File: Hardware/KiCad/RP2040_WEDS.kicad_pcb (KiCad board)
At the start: 2 copper layers, 55 x 66 mm, 75 parts, among them J1 Barrel_Jack_Switch_Pin3Ring, J2 Conn_01x02_Male, J3 I2C Soil Header, J4 LiPo Batt, J5 Analog Soil Header, J6 USB Header, J7 Conn_02x05_Odd_Even, J8 SMA-J-P-H-RA-TH1, Q1 Q_PMOS_DGS, Q2 Q_PMOS_DGS, SW1 SW_Push, SW2 SW_Push, SW3 SW_Push, U1 RP2040, U2 MCP73831-2-OT, U3 W25Q128JVS, U4 BME280, U5 AP2112K-3.3, U6 LoRa-E5, U7 TPL5110, Y1 Crystal_GND24

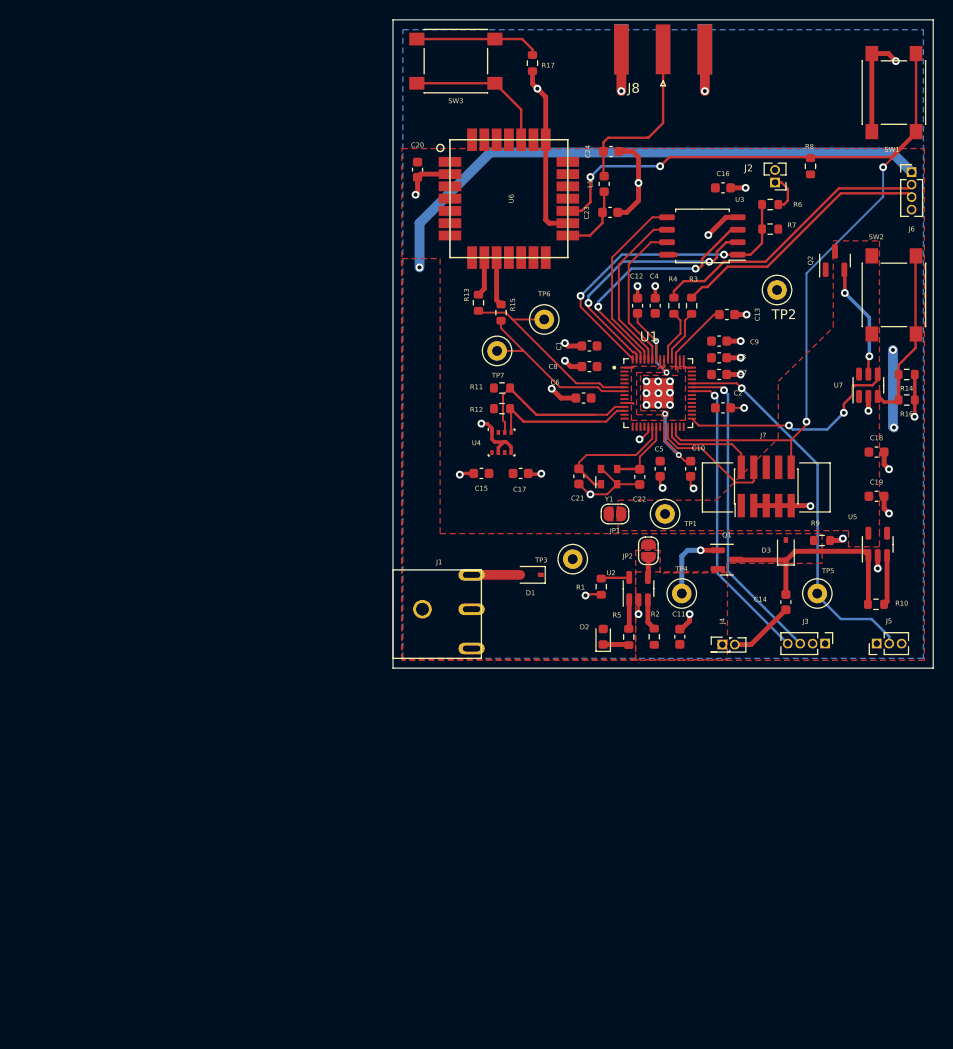
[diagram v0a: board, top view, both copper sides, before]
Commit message: added thermal relief to fill zones
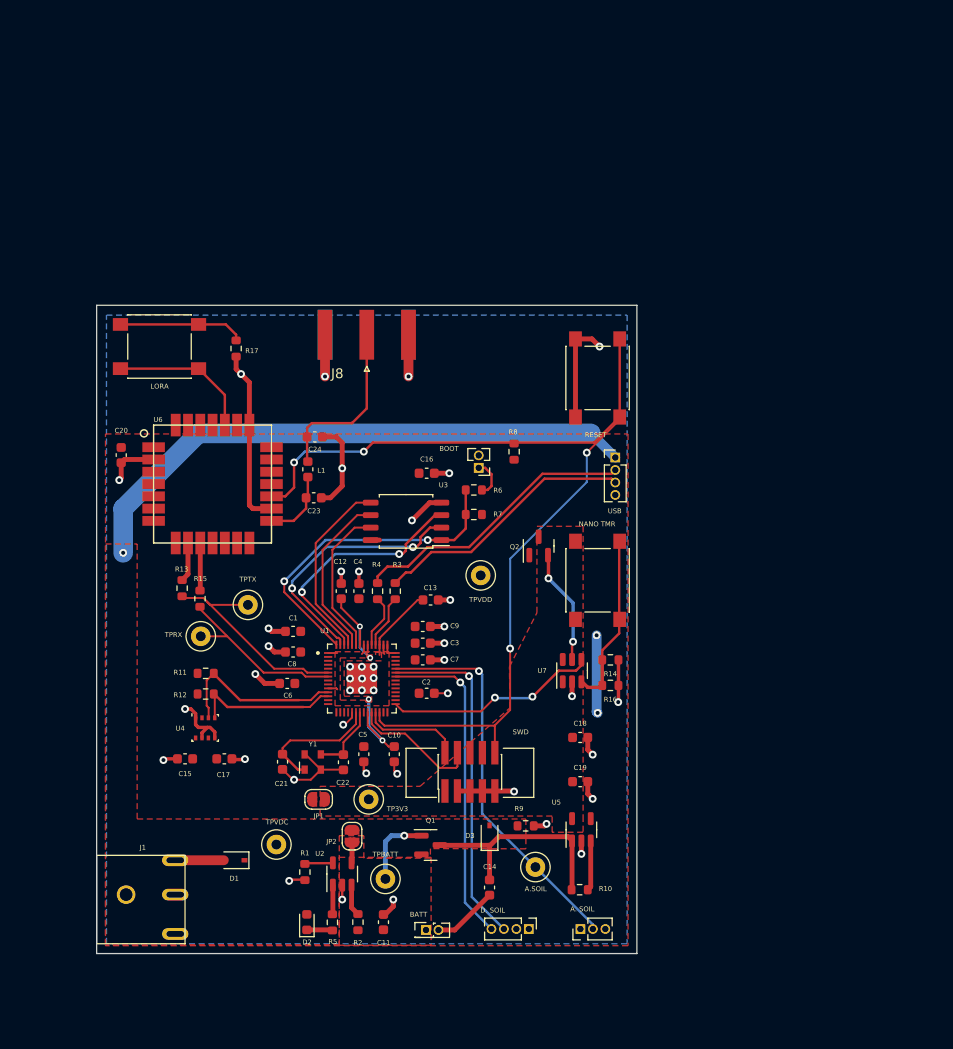
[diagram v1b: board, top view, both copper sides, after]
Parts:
- A. SOIL: renamed from J5
- D. SOIL: renamed from J3
- NANO TMR: renamed from SW2
- moved R15 42.3 mm to (130.3, 97.9)
- moved BOOT 41.9 mm to (158.7, 84.6)
- moved C12 41.9 mm to (144.7, 97.2)
- moved C21 41.9 mm to (138.8, 114.5)
- moved C6 41.9 mm to (139.2, 106.6)
- moved R10 41.9 mm to (169.0, 127.6)
- moved R14 41.9 mm to (172.1, 104.2)
- moved R3 41.9 mm to (150.2, 97.2)
- moved R6 41.9 mm to (158.2, 86.9)
- moved R7 41.9 mm to (158.2, 89.4)
- moved R9 41.9 mm to (163.5, 121.1)
- moved TPTX 41.9 mm to (135.2, 98.6)
- moved USB 41.9 mm to (172.6, 83.6)
- moved C10 41.9 mm to (150.1, 113.8)
- moved C20 41.9 mm to (122.3, 83.3)
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- renumbered TP5 to A.SOIL, J4 to BATT, J2 to BOOT, SW3 to LORA, SW1 to RESET, J7 to SWD, TP1 to TP3V3, TP4 to TPBATT, TP7 to TPRX, TP6 to TPTX, TP3 to TPVDC, TP2 to TPVDD, J6 to USB
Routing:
- net SCL_SOIL: track 32.4 -> 34.8 mm
- net SDA_SOIL: track 30.8 -> 33.2 mm
- net DONE: track 23.0 -> 21.8 mm
- net LORA_TX: track 21.3 -> 22.4 mm

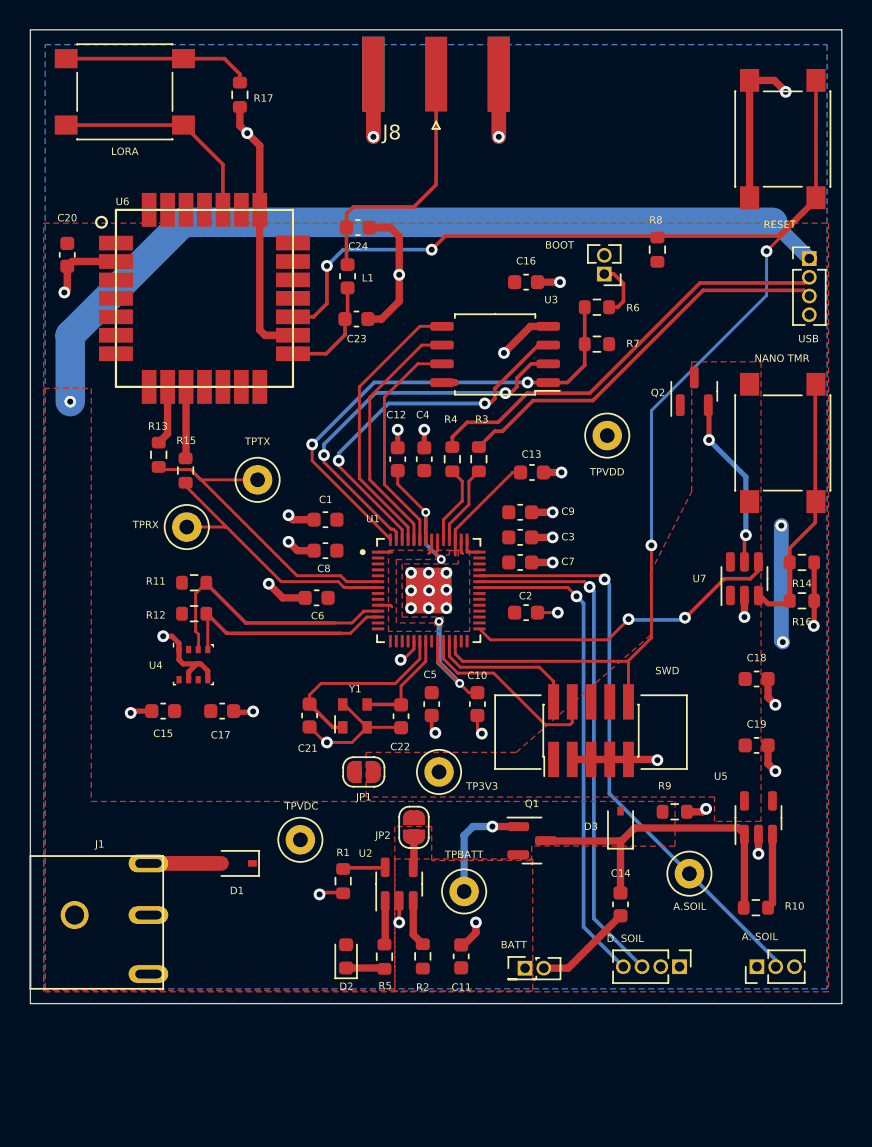
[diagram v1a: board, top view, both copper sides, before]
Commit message: changed the size of headers form 1.27 to 2.54mm
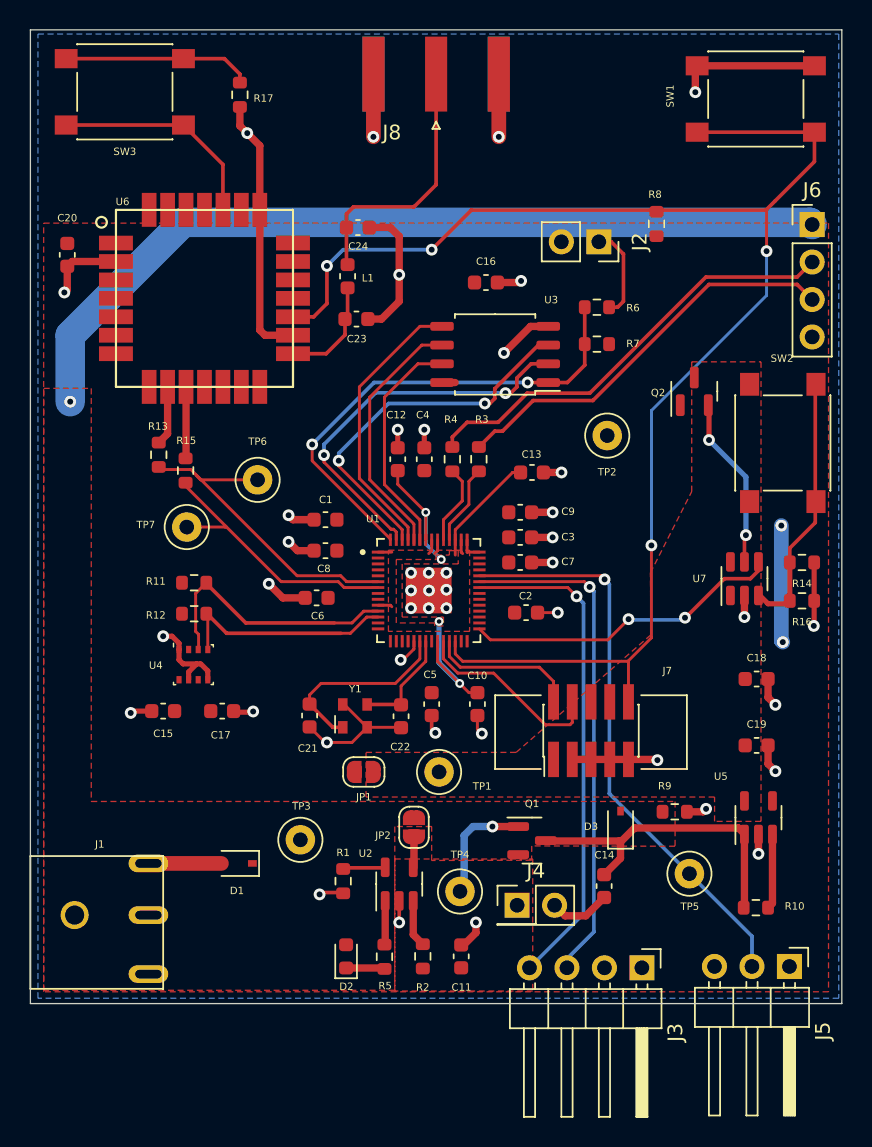
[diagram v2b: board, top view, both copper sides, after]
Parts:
- J2: renamed from BOOT; footprint Connector_PinHeader_1.27mm:PinHeader_1x02_P1.27mm_Vertical -> Connector_PinSocket_2.54mm:PinSocket_1x02_P2.54mm_Vertical
- J3: renamed from D. SOIL; footprint Connector_PinHeader_1.27mm:PinHeader_1x04_P1.27mm_Vertical -> Connector_PinHeader_2.54mm:PinHeader_1x04_P2.54mm_Horizontal
- J4: renamed from BATT; footprint Connector_PinHeader_1.27mm:PinHeader_2x01_P1.27mm_Vertical -> Connector_PinHeader_2.54mm:PinHeader_2x01_P2.54mm_Vertical
- J5: renamed from A. SOIL; footprint Connector_PinHeader_1.27mm:PinHeader_1x03_P1.27mm_Vertical -> Connector_PinHeader_2.54mm:PinHeader_1x03_P2.54mm_Horizontal
- J6: renamed from USB; footprint Connector_PinHeader_1.27mm:PinHeader_1x04_P1.27mm_Vertical -> Connector_PinHeader_2.54mm:PinHeader_1x04_P2.54mm_Vertical
- SW2: renamed from NANO TMR
- moved J4 4.30 mm to (152.8, 127.4)
- moved SW1 3.27 mm to (169.0, 72.7), turned to 180 degrees
- moved C16 2.72 mm to (150.7, 85.2)
- moved J3 2.55 mm to (161.3, 131.6)
- moved J6 2.31 mm to (172.8, 81.2)
- moved J2 2.22 mm to (158.4, 82.4), turned to -90 degrees
- moved J5 2.20 mm to (171.3, 131.5), turned to -90 degrees
- moved R8 1.75 mm to (162.3, 81.2)
- moved C14 1.66 mm to (158.7, 126.1)
- moved TP4 0.28 mm to (148.9, 126.5)
- renumbered SWD to J7, RESET to SW1, LORA to SW3, TP3V3 to TP1, TPVDD to TP2, TPVDC to TP3, TPBATT to TP4, A.SOIL to TP5, TPTX to TP6, TPRX to TP7
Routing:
- net GND: track 127.4 -> 124.1 mm
- net /~{USB_BOOT}: track 3.91 -> 6.36 mm
- net RESET: track 100.5 -> 102.0 mm
- net Net-(C14-Pad1): track 22.5 -> 21.7 mm
- net VDC: track 58.8 -> 58.0 mm
- net SOIL_SIG: track 39.6 -> 39.0 mm
- net USB_DP: track 29.4 -> 30.0 mm
- net USB_DN: track 27.0 -> 27.6 mm
- net SCL_SOIL: track 34.8 -> 34.3 mm

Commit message: fixed component values
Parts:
- removed JP2: SolderJumper_2_Open, Jumper:SolderJumper-2_P1.3mm_Open_RoundedPad1.0x1.5mm
- removed R10: 10k, Resistor_SMD:R_0603_1608Metric
- removed R2: 0, Resistor_SMD:R_0603_1608Metric
- removed TP4, TP5: TestPoint, TestPoint:TestPoint_Loop_D1.80mm_Drill1.0mm_Beaded
- added J9: Solar, Connector_PinHeader_2.54mm:PinHeader_1x02_P2.54mm_Horizontal, F.Cu at (122.2, 119.9)
- C11, C19: value 10uF -> 4.7uF
- C18: value 10uF -> 1uF
- J4: moved to B.Cu
- R5: value 10k -> 470
- U5: value AP2112K-3.3 -> XC6210B332MR
- moved C19 24.8 mm to (144.9, 122.0), turned to 180 degrees
- moved TP3 7.94 mm to (134.1, 129.8)
- moved D2 7.48 mm to (139.4, 123.6)
- moved J4 7.32 mm to (146.7, 131.4), turned to 180 degrees
- moved C14 7.01 mm to (165.4, 124.0), turned to 90 degrees
- moved R5 5.66 mm to (140.5, 126.3), turned to 0 degrees
- moved C18 5.09 mm to (170.3, 117.0)
- moved C11 4.84 mm to (144.7, 128.7), turned to 180 degrees
- moved Q1 2.96 mm to (151.7, 125.0), turned to 180 degrees
- moved J7 2.95 mm to (160.8, 115.5)
- moved R1 2.19 mm to (141.4, 123.6), turned to -90 degrees
- moved D3 2.01 mm to (159.2, 124.0)
- moved R9 1.60 mm to (162.0, 121.7)
- moved J2 1.38 mm to (158.3, 83.8)
- moved U5 1.22 mm to (170.3, 121.0)
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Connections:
- C19 pad 1: +3V3 -> VDC
- U2 pad 3: Net-(R2-Pad2) -> +BATT
- U2 pad 4: Net-(JP2-Pad1) -> VDC
- U5 pad 3: Net-(R10-Pad1) -> Net-(C14-Pad1)
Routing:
- net +BATT: track 7.76 -> 0.00 mm, vias 1 -> 0
- net Net-(R10-Pad1): track 5.12 -> 0.00 mm
- net Net-(R2-Pad2): track 3.24 -> 0.00 mm
- net +3V3: track 0.14 -> 3.14 mm
- net SWD_CLK: track 13.2 -> 15.9 mm
- net Net-(C14-Pad1): track 21.7 -> 23.9 mm
- net RESET: track 102.0 -> 104.1 mm
- net SWD_DIO: track 10.2 -> 12.3 mm
- net Net-(JP2-Pad1): track 2.05 -> 0.00 mm
- net VDC: track 58.0 -> 60.0 mm
- net /~{USB_BOOT}: track 6.36 -> 4.51 mm
- net GND: track 124.1 -> 122.8 mm, vias 44 -> 42
- net Net-(D2-Pad1): track 2.73 -> 2.03 mm
- net Net-(R5-Pad2): track 3.02 -> 2.45 mm

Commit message: Version 1.2 board
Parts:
- removed J1: Barrel_Jack_Switch_Pin3Ring, 54-00125:54-00125
- added D4: LED, LED_SMD:LED_0603_1608Metric, F.Cu at (125.5, 131.3)
- added R10: 0, Resistor_SMD:R_0603_1608Metric, F.Cu at (148.0, 123.4)
- added R18: 0, Resistor_SMD:R_0603_1608Metric, F.Cu at (160.7, 128.6)
- added R19: 0, Resistor_SMD:R_0603_1608Metric, F.Cu at (170.5, 128.6)
- added R2: 0, Resistor_SMD:R_0603_1608Metric, F.Cu at (148.1, 127.8)
- added R20: 0, Resistor_SMD:R_0603_1608Metric, F.Cu at (122.2, 94.4)
- added R21: 0, Resistor_SMD:R_0603_1608Metric, F.Cu at (169.1, 117.1)
- added R22: 470, Resistor_SMD:R_0603_1608Metric, F.Cu at (122.3, 131.3)
- added TP4: GND, TestPoint:TestPoint_Loop_D1.80mm_Drill1.0mm_Beaded, F.Cu at (130.5, 131.5)
- added TP5: 1V1, TestPoint:TestPoint_Loop_D1.80mm_Drill1.0mm_Beaded, F.Cu at (158.9, 95.4)
- added TP8: Q1, TestPoint:TestPoint_Loop_D1.80mm_Drill1.0mm_Beaded, F.Cu at (160.8, 125.0)
- J2: value Conn_01x02_Male -> USB BOOT
- J7: value Conn_02x05_Odd_Even -> SWD Header; footprint Connector_PinHeader_1.27mm:PinHeader_2x05_P1.27mm_Vertical_SMD -> Connector_PinHeader_1.27mm:PinHeader_2x05_P1.27mm_Vertical
- J8: value SMA-J-P-H-RA-TH1 -> SMA-Conn
- J9: value Solar -> Solar Panel Input; moved to B.Cu
- JP1: value SolderJumper_2_Open -> Power Isolation
- R11, R12: value 10k -> 4.7k
- TP1: value TestPoint -> 3V3
- TP2: value TestPoint -> VDD
- TP3: value TestPoint -> VDC
- TP6: value TestPoint -> LoRa_TX
- TP7: value TestPoint -> LoRa_RX
- moved R9 9.99 mm to (152.0, 121.3), turned to 180 degrees
- moved C17 9.06 mm to (126.3, 107.9), turned to 90 degrees
- moved D2 7.85 mm to (140.9, 131.3)
- moved TP2 5.75 mm to (158.9, 101.3)
- moved R5 5.30 mm to (138.7, 131.3), turned to 90 degrees
- moved R12 5.16 mm to (134.1, 111.7)
- moved J9 4.68 mm to (122.2, 124.6)
- moved R11 4.14 mm to (134.1, 108.2)
- moved TP7 3.79 mm to (133.7, 103.6)
- moved C15 3.48 mm to (126.3, 111.8), turned to -90 degrees
- moved J7 3.21 mm to (163.5, 117.2), turned to 180 degrees
- moved C18 3.03 mm to (169.1, 114.2)
- moved D3 3.01 mm to (156.1, 123.9)
- moved TP3 2.00 mm to (135.1, 131.5)
- moved U4 1.73 mm to (129.6, 109.9), turned to -90 degrees
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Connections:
- C9 pad 1: VDD -> GND
- C9 pad 2: GND -> VDD
- D1 pad 2: Net-(D1-Pad2) -> Net-(J9-Pad1)
- D2 pad 2: VDC -> Net-(U2-Pad1)
- J3 pad 1: VDD -> Net-(J3-Pad1)
- J5 pad 1: VDD -> Net-(J5-Pad1)
- J6 pad 1: VDC -> Net-(J6-Pad1)
- J9 pad 1: VDC -> Net-(J9-Pad1)
- R5 pad 2: Net-(R5-Pad2) -> GND
- U1 pad 4: unconnected-(U1-Pad4) -> NRST
- U2 pad 1: Net-(R5-Pad2) -> Net-(U2-Pad1)
- U2 pad 3: +BATT -> Net-(U2-Pad3)
- U2 pad 4: VDC -> Net-(U2-Pad4)
- U5 pad 5: +3V3 -> Net-(U5-Pad5)
- U6 pad 17: RESET -> NRST
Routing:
- net VDC: track 60.0 -> 0.00 mm, vias 1 -> 0
- net Net-(J6-Pad1): track 0.00 -> 57.1 mm, vias 0 -> 1
- net RESET: track 104.1 -> 71.4 mm, vias 4 -> 2
- net NRST: track 0.00 -> 23.1 mm, vias 0 -> 2
- net Net-(J9-Pad1): track 0.00 -> 10.6 mm
- net +1V1: track 26.6 -> 33.6 mm
- net Net-(U2-Pad1): track 0.00 -> 6.22 mm
- net SWD_DIO: track 12.3 -> 17.8 mm, vias 0 -> 1
- net Net-(D1-Pad2): track 4.95 -> 0.00 mm
- net SDA: track 18.0 -> 13.9 mm
- net GND: track 122.8 -> 118.8 mm, vias 42 -> 44
- net Net-(D4-Pad1): track 0.00 -> 3.22 mm
- net Net-(U5-Pad5): track 0.00 -> 3.03 mm
- net +3V3: track 3.14 -> 0.14 mm
- net Net-(J5-Pad1): track 0.00 -> 2.99 mm
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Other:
- board text added: "+"
- board text added: "1"
- board text added: "D+"
- board text added: "D-"
- board text added: "FULL"
- board text added: "GND"
- board text added: "POWER"
- board text added: "VDC"
- board text added: "WildEDS v1.2 Baldeep Pannu Joss Chandler"
- board text removed: "Joss Chandler Baldeep Pannu"
- board text removed: "Western Washinton University"
- board text removed: "WildEDS v1.00"

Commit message: v1.2
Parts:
- added G***: LOGO, 54-00125:Logo, B.Cu at (148.7, 130.2)
- moved SW3 20.4 mm to (123.4, 92.5), turned to -90 degrees
- moved R17 17.9 mm to (122.0, 85.7), turned to 180 degrees
- moved J2 12.0 mm to (158.3, 71.8), turned to 90 degrees
- moved U6 9.64 mm to (130.3, 76.7)
- moved C20 9.63 mm to (121.6, 73.7)
- moved R15 9.27 mm to (129.4, 88.7)
- moved R13 8.99 mm to (127.7, 87.9)
- moved R20 8.40 mm to (122.2, 102.8)
- moved U3 7.99 mm to (143.3, 89.9), turned to 0 degrees
- moved R7 7.53 mm to (151.5, 85.9)
- moved R6 7.31 mm to (151.5, 83.9)
- moved C23 6.48 mm to (141.8, 81.2), turned to -90 degrees
- moved L1 5.41 mm to (144.5, 80.4), turned to 0 degrees
- moved C24 5.32 mm to (147.3, 81.2), turned to -90 degrees
- moved R8 4.76 mm to (165.2, 77.5), turned to 0 degrees
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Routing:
- net GND: track 118.8 -> 95.8 mm, vias 44 -> 46
- net Net-(U6-Pad24): track 14.8 -> 28.2 mm
- net NRST: track 23.1 -> 34.7 mm, vias 2 -> 0
- net /~{USB_BOOT}: track 4.51 -> 14.6 mm
- net LORA_RX: track 18.3 -> 27.4 mm
- net QSPI_SD2: track 25.3 -> 16.2 mm, vias 2 -> 0
- net QSPI_SD1: track 26.4 -> 17.9 mm, vias 2 -> 0
- net RESET: track 71.4 -> 63.8 mm
- net Net-(C24-Pad1): track 17.9 -> 11.4 mm
- net LORA_TX: track 21.3 -> 27.6 mm
- net QSPI_SD3: track 15.8 -> 20.2 mm
- net QSPI_SD0: track 19.0 -> 15.3 mm
- net Net-(J6-Pad1): track 57.1 -> 60.5 mm
- net Net-(R17-Pad2): track 12.8 -> 10.8 mm
- net USB_DN: track 27.6 -> 29.2 mm
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
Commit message: v1.2
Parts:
- moved R7 13.6 mm to (137.9, 85.7), turned to 180 degrees
- moved R6 9.64 mm to (142.1, 85.7)
- moved Q2 3.25 mm to (164.9, 95.8)
- moved C16 1.78 mm to (149.8, 88.3), turned to -90 degrees
- moved C24 1.70 mm to (145.6, 81.3)
- moved C23 1.60 mm to (140.2, 81.3)
- moved L1 1.60 mm to (142.9, 80.5)
- moved J2 1.49 mm to (157.2, 70.8)
- moved TP2 1.13 mm to (159.7, 102.1)
- moved U3 1.08 mm to (142.3, 90.3)
- moved TP5 0.94 mm to (159.7, 95.9)
- moved C3 0.85 mm to (153.8, 102.2)
- moved C7 0.85 mm to (153.8, 103.9)
- moved C9 0.85 mm to (153.8, 100.5)
- moved SW2 0.54 mm to (170.8, 96.6)
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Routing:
- net /~{USB_BOOT}: track 14.6 -> 25.4 mm
- net QSPI_CSN: track 33.6 -> 23.8 mm
- net RESET: track 63.8 -> 69.1 mm
- net Net-(Q2-Pad2): track 11.7 -> 8.43 mm, vias 2 -> 0
- net GND: track 95.8 -> 93.2 mm
- net QSPI_SD3: track 20.2 -> 18.2 mm
- net QSPI_CLK: track 18.9 -> 17.0 mm
- net Net-(C23-Pad1): track 7.43 -> 5.85 mm
- net QSPI_SD0: track 15.3 -> 13.7 mm
- net QSPI_SD2: track 16.2 -> 14.7 mm
- net QSPI_SD1: track 17.9 -> 16.7 mm
- net USB_DN: track 29.2 -> 28.1 mm
- net +1V1: track 33.2 -> 34.0 mm
- net Net-(C24-Pad1): track 11.4 -> 12.1 mm
- net LORA_TX: track 27.6 -> 28.1 mm
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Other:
- board text added: "LORA"
- board text added: "NANO"
- board text added: "RESET"
